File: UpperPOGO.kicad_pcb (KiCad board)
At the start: 2 copper layers, 128 x 59.3 mm, 29 parts, among them J1 Conn_01x01_MountingPin, J10 Conn_01x01_MountingPin, J11 Conn_01x01_MountingPin, J12 Conn_01x01_MountingPin, J13 Conn_01x01_MountingPin, J14 Conn_01x01_MountingPin, J15 Conn_01x01_MountingPin, J16 Conn_01x01_MountingPin, J17 Conn_01x01_MountingPin, J18 Conn_01x01_MountingPin, J19 Conn_01x01_MountingPin, J2 Conn_01x01_MountingPin, J20 Conn_01x01_MountingPin, J21 Conn_01x01_MountingPin, J22 Conn_01x01_MountingPin, J23 Conn_01x01_MountingPin, J24 Conn_01x01_MountingPin, J25 Conn_02x12_Pin, J3 Conn_01x01_MountingPin, J4 Conn_01x01_MountingPin, J5 Conn_01x01_MountingPin, J6 Conn_01x01_MountingPin, J7 Conn_01x01_MountingPin, J8 Conn_01x01_MountingPin, J9 Conn_01x01_MountingPin

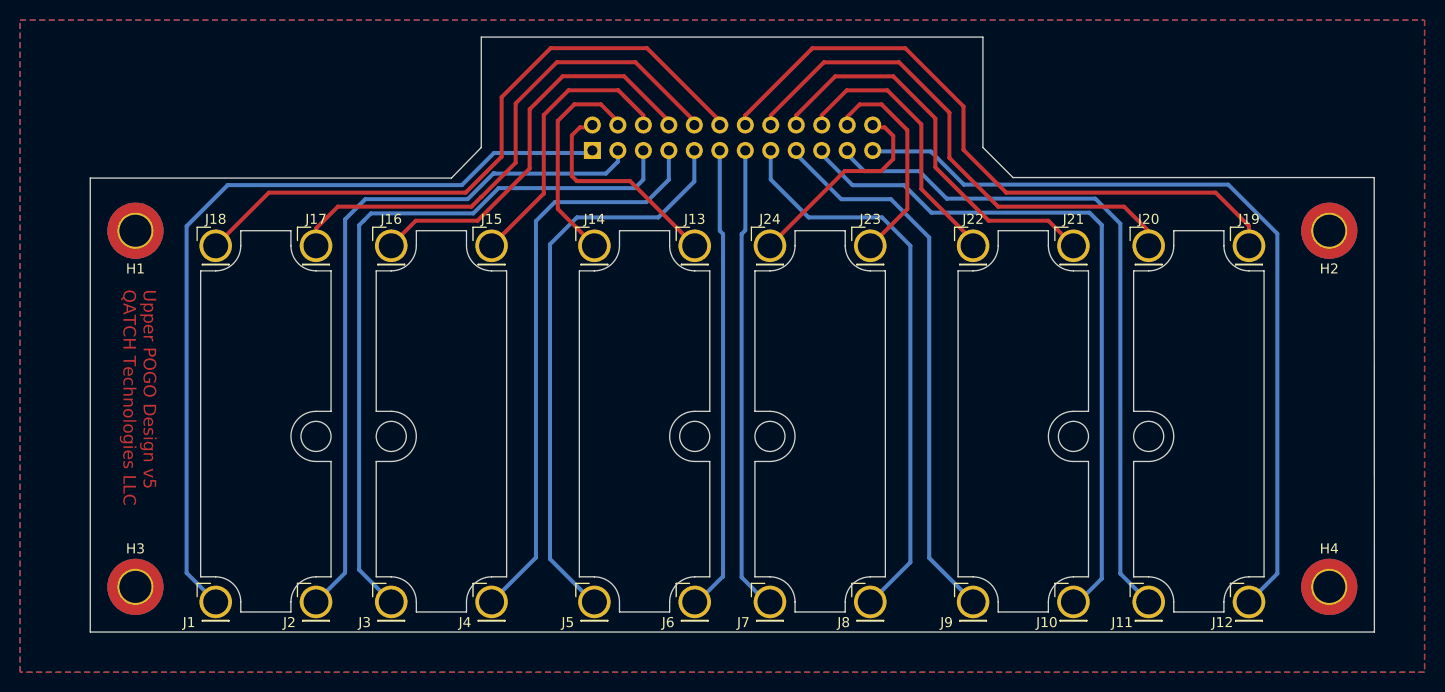
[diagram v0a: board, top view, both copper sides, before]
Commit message: Multiport Design for UpperPOGO v7 Update fabrication output files
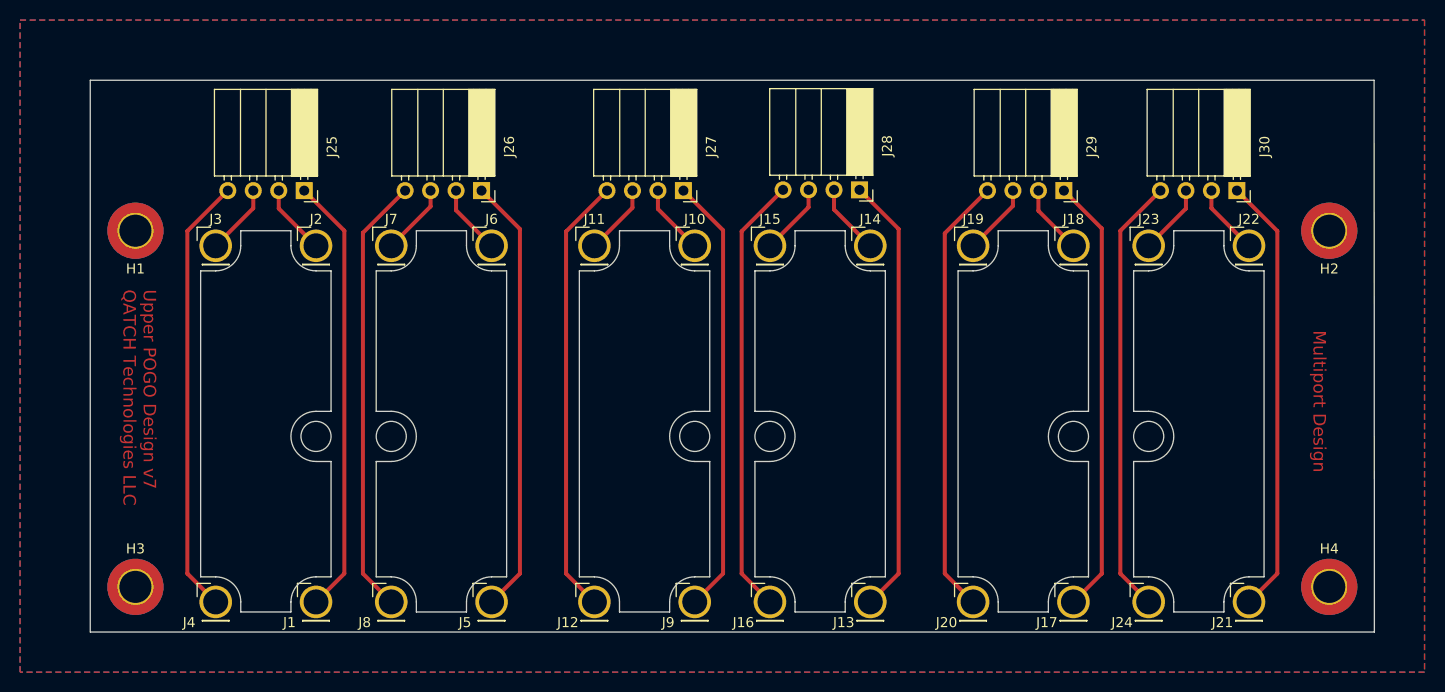
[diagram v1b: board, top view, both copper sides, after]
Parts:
- added J26: Conn_01x04_Pin, Connector_PinSocket_2.54mm:PinSocket_1x04_P2.54mm_Horizontal, F.Cu at (121.0, 62.0)
- added J27: Conn_01x04_Pin, Connector_PinSocket_2.54mm:PinSocket_1x04_P2.54mm_Horizontal, F.Cu at (141.1, 62.0)
- added J28: Conn_01x04_Pin, Connector_PinSocket_2.54mm:PinSocket_1x04_P2.54mm_Horizontal, F.Cu at (158.7, 61.9)
- added J29: Conn_01x04_Pin, Connector_PinSocket_2.54mm:PinSocket_1x04_P2.54mm_Horizontal, F.Cu at (179.1, 62.0)
- added J30: Conn_01x04_Pin, Connector_PinSocket_2.54mm:PinSocket_1x04_P2.54mm_Horizontal, F.Cu at (196.3, 62.0)
- J25: value Conn_02x12_Pin -> Conn_01x04_Pin; footprint Connector_PinSocket_2.54mm:PinSocket_2x12_P2.54mm_Vertical -> Connector_PinSocket_2.54mm:PinSocket_1x04_P2.54mm_Horizontal; moved to F.Cu
- moved J25 29.0 mm to (103.3, 62.0)
- renumbered J2 to J1, J13 to J10, J14 to J11, J5 to J12, J8 to J13, J23 to J14, J24 to J15, J7 to J16, J10 to J17, J21 to J18, J22 to J19, J17 to J2, J9 to J20, J12 to J21, J19 to J22, J20 to J23, J11 to J24, J18 to J3, J1 to J4, J4 to J5, J15 to J6, J16 to J7, J3 to J8, J6 to J9
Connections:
- J1 pad 1: Net-(J2-Pin_1) -> Net-(J1-Pin_1)
- J10 pad 1: Net-(J13-Pin_1) -> Net-(J10-Pin_1)
- J11 pad 1: Net-(J14-Pin_1) -> Net-(J11-Pin_1)
- J12 pad 1: Net-(J25-Pin_5) -> Net-(J12-Pin_1)
- J13 pad 1: Net-(J25-Pin_8) -> Net-(J13-Pin_1)
- J14 pad 1: Net-(J23-Pin_1) -> Net-(J14-Pin_1)
- J15 pad 1: Net-(J24-Pin_1) -> Net-(J15-Pin_1)
- J16 pad 1: Net-(J25-Pin_7) -> Net-(J16-Pin_1)
- J17 pad 1: Net-(J10-Pin_1) -> Net-(J17-Pin_1)
- J18 pad 1: Net-(J21-Pin_1) -> Net-(J18-Pin_1)
- J19 pad 1: Net-(J22-Pin_1) -> Net-(J19-Pin_1)
- J2 pad 1: Net-(J17-Pin_1) -> Net-(J2-Pin_1)
- J20 pad 1: Net-(J25-Pin_9) -> Net-(J20-Pin_1)
- J21 pad 1: Net-(J12-Pin_1) -> Net-(J21-Pin_1)
- J22 pad 1: Net-(J19-Pin_1) -> Net-(J22-Pin_1)
- J23 pad 1: Net-(J20-Pin_1) -> Net-(J23-Pin_1)
- J24 pad 1: Net-(J11-Pin_1) -> Net-(J24-Pin_1)
- J3 pad 1: Net-(J18-Pin_1) -> Net-(J25-Pin_3)
- J4 pad 1: Net-(J1-Pin_1) -> Net-(J25-Pin_4)
- J5 pad 1: Net-(J25-Pin_4) -> Net-(J26-Pin_1)
- J6 pad 1: Net-(J15-Pin_1) -> Net-(J26-Pin_2)
- J7 pad 1: Net-(J16-Pin_1) -> Net-(J26-Pin_3)
- J8 pad 1: Net-(J25-Pin_3) -> Net-(J26-Pin_4)
- J9 pad 1: Net-(J25-Pin_6) -> Net-(J27-Pin_1)
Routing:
- net Net-(J25-Pin_3): track 71.7 -> 7.05 mm
- net Net-(J2-Pin_1): track 70.1 -> 7.04 mm
- net Net-(J10-Pin_1): track 69.5 -> 7.02 mm
- net Net-(J11-Pin_1): track 68.9 -> 7.07 mm
- net Net-(J19-Pin_1): track 65.8 -> 7.14 mm
- net Net-(J18-Pin_1): track 65.5 -> 6.95 mm
- net Net-(J25-Pin_5): track 57.4 -> 0.00 mm
- net Net-(J25-Pin_8): track 56.4 -> 0.00 mm
- net Net-(J25-Pin_9): track 54.8 -> 0.00 mm
- net Net-(J25-Pin_7): track 46.3 -> 0.00 mm
- net Net-(J25-Pin_6): track 46.0 -> 0.00 mm
- net Net-(J26-Pin_4): track 0.00 -> 43.9 mm
- net Net-(J27-Pin_1): track 0.00 -> 43.8 mm
- net Net-(J26-Pin_1): track 0.00 -> 43.8 mm
- net Net-(J1-Pin_1): track 86.4 -> 43.8 mm
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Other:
- board size 128 x 59.3 mm -> 128 x 55 mm
- board text added: "Multiport Design"
- board text added: "Upper POGO Design v7 QATCH Technologies LLC"
- board text removed: "Upper POGO Design v5 QATCH Technologies LLC"

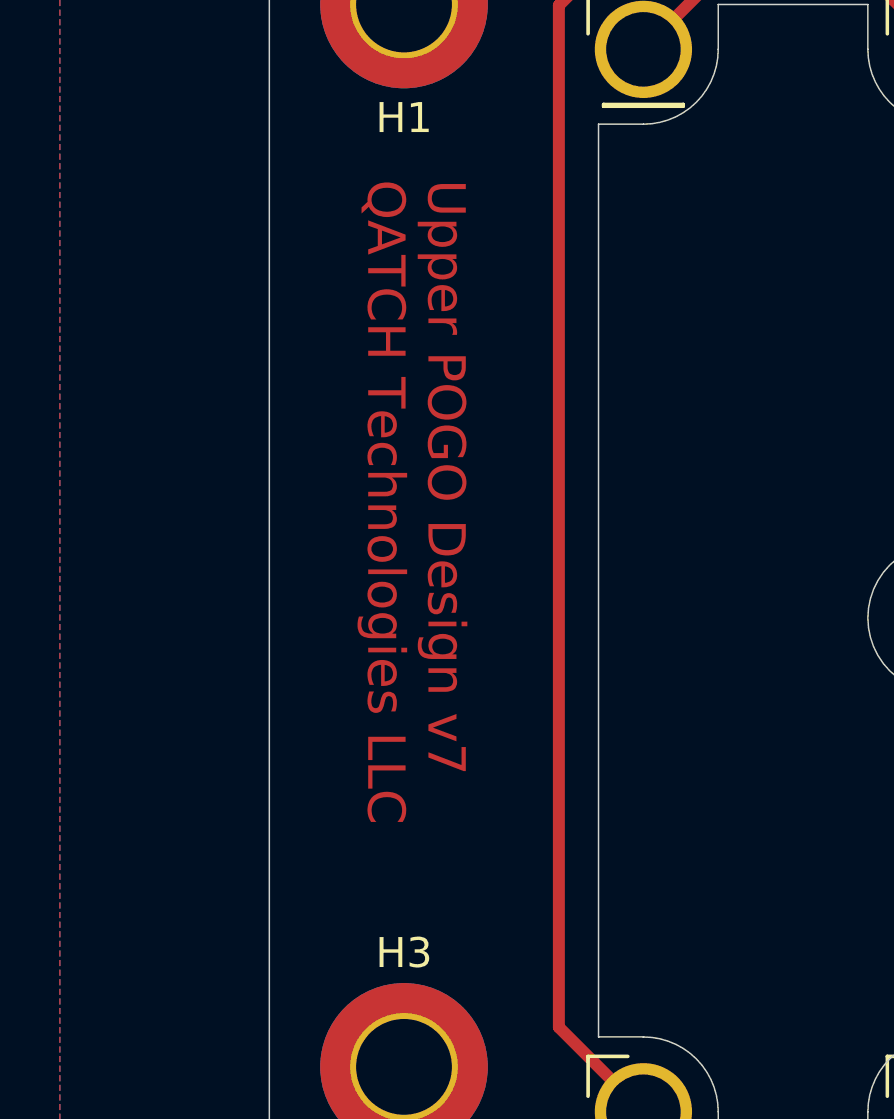
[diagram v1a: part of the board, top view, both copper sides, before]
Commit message: v8 Changes: - Update version to match lowerPOGO design - No other changes for upperPOGO.
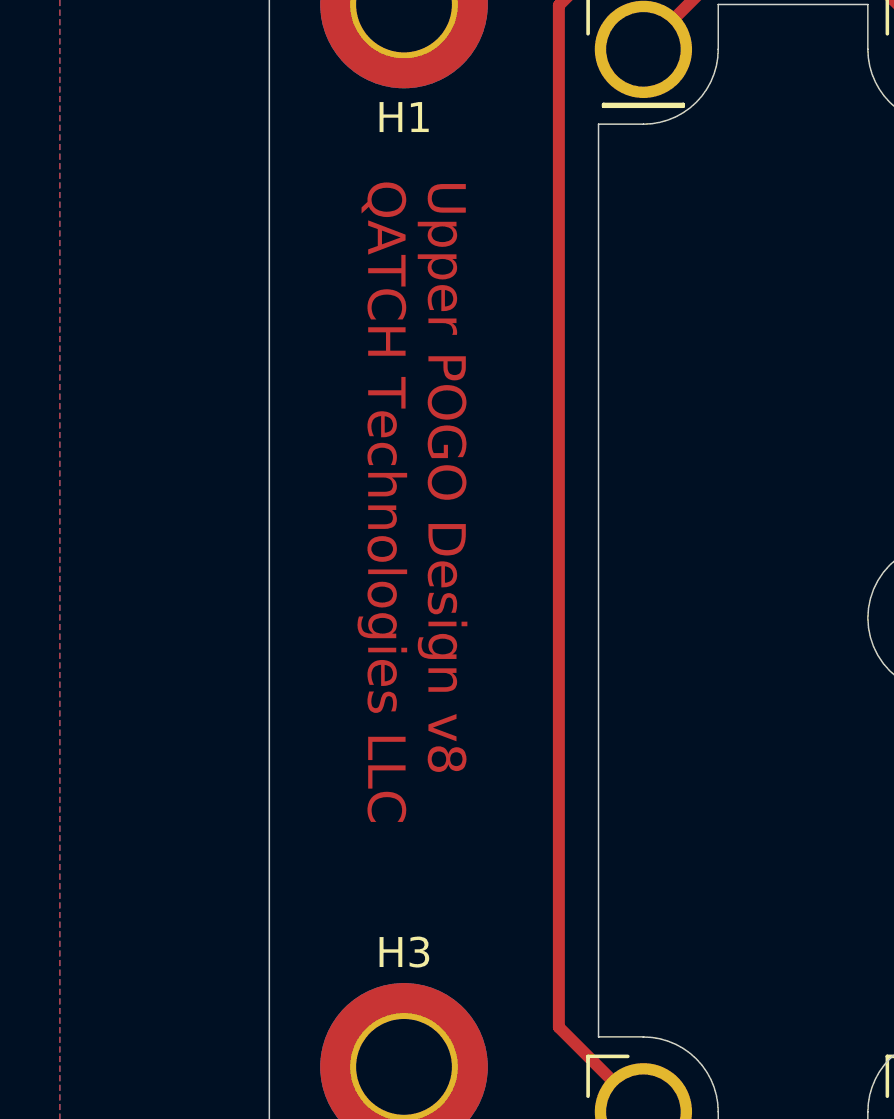
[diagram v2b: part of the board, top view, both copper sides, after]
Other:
- board text added: "Upper POGO Design v8 QATCH Technologies LLC"
- board text removed: "Upper POGO Design v7 QATCH Technologies LLC"
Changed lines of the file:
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@@
 		)
 	)
-	(gr_text "Upper POGO Design v7\nQATCH Technologies LLC"
+	(gr_text "Upper POGO Design v8\nQATCH Technologies LLC"
 		(at 85.15 71.85 270)
 		(layer "F.Cu" knockout)
